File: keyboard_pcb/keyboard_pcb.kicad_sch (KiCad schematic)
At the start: 1 part

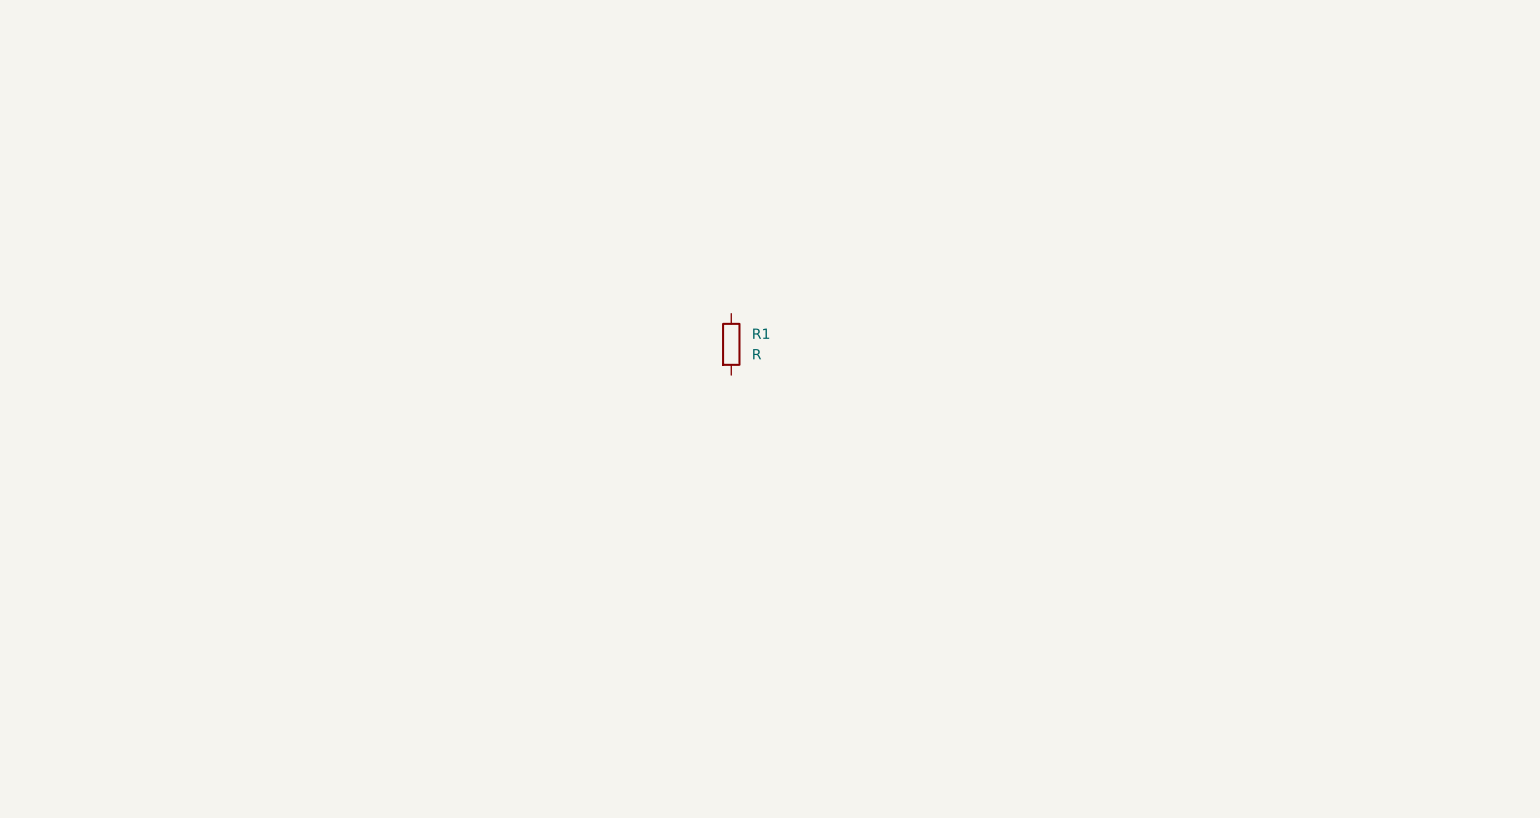
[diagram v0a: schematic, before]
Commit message: Schematic Completed, PCB drawing
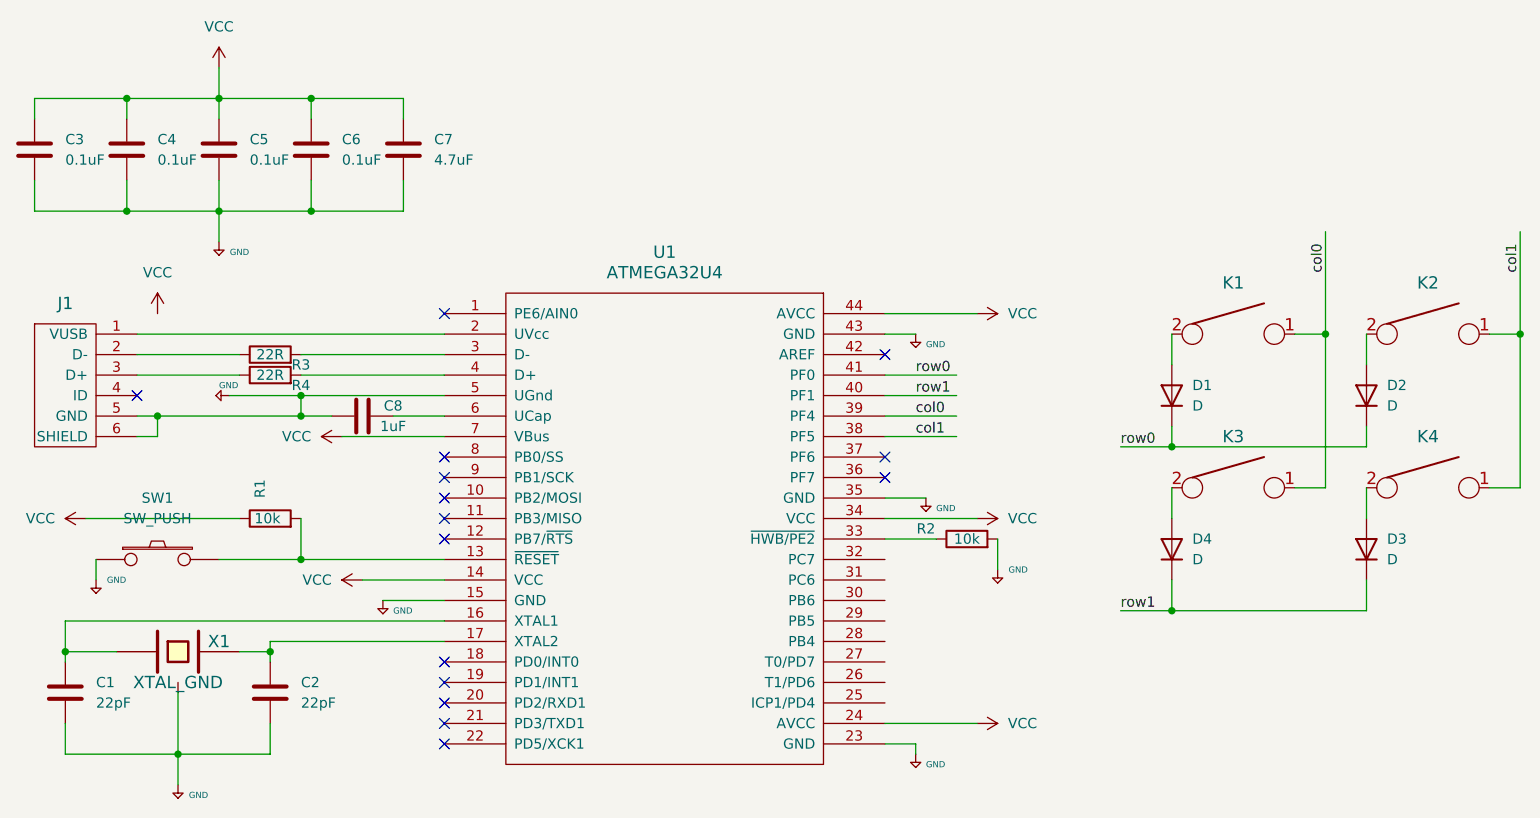
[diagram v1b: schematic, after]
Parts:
- added C1, C2: 22pF, Capacitor_SMD:C_0805_2012Metric_Pad1.18x1.45mm_HandSolder, symbol Device:C
- added C3, C4, C5, C6: 0.1uF, Capacitor_SMD:C_0805_2012Metric_Pad1.18x1.45mm_HandSolder, symbol Device:C
- added C7: 4.7uF, Capacitor_SMD:C_0805_2012Metric_Pad1.18x1.45mm_HandSolder, symbol Device:C
- added C8: 1uF, Capacitor_SMD:C_0805_2012Metric_Pad1.18x1.45mm_HandSolder, symbol Device:C
- added D1, D2, D3, D4: D, keyboard_parts:D_SOD123_axial, symbol Device:D
- added J1: USB_mini_micro_B, keyboard_parts:USB_miniB_hirose_5S8, symbol keyboard_parts:USB_mini_micro_B
- added K1, K2, K3, K4: KEYSW, keebs:Mx_Alps_100, symbol keyboard_parts:KEYSW
- added R2: 10k, Resistor_SMD:R_0805_2012Metric_Pad1.20x1.40mm_HandSolder, symbol Device:R
- added R3, R4: 22R, Resistor_SMD:R_0805_2012Metric_Pad1.20x1.40mm_HandSolder, symbol Device:R
- added SW1: SW_PUSH, Button_Switch_SMD:SW_SPST_TL3342, symbol keyboard_parts:SW_PUSH
- added U1: ATMEGA32U4, Package_QFP:LQFP-44_10x10mm_P0.8mm, symbol keyboard_parts:ATMEGA32U4
- added X1: XTAL_GND, Crystal:Crystal_SMD_3225-4Pin_3.2x2.5mm_HandSoldering, symbol keyboard_parts:XTAL_GND
- R1: value R -> 10k; footprint (none) -> Resistor_SMD:R_0805_2012Metric_Pad1.20x1.40mm_HandSolder
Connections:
- net VCC: now reaches R1.1
- net VCC: now also C3.1, C4.1, C5.1, C6.1, C7.1, U1.14 (VCC), U1.24 (AVCC), U1.34 (VCC), U1.44 (AVCC), U1.7 (VBus)
- net at R1.2: now also SW1.2, U1.13 (~{RESET})
- new net: D1.2 (A), K1.2
- new net: D2.2 (A), K2.2
- new net: C2.1, U1.17 (XTAL2), X1.2
- new net: D4.2 (A), K3.2
- new net: R2.1, U1.33 (~{HWB/PE2})
- new net: D3.2 (A), K4.2
- new net: J1.2 (D-), R3.1
- new net: R3.2, U1.3 (D-)
- new net: C1.1, U1.16 (XTAL1), X1.1
- new net: J1.1 (VUSB), U1.2 (UVcc)
- new net: J1.3 (D+), R4.1
- new net: R4.2, U1.4 (D+)
- new net: C8.2, U1.6 (UCap)
- new net +5V: C1.2, C2.2, C3.2, C4.2, C5.2, C6.2, C7.2, C8.1, J1.5 (GND), J1.6 (SHIELD), R2.2, SW1.1, U1.15 (GND), U1.23 (GND), U1.35 (GND), U1.43 (GND), U1.5 (UGnd), X1.3
- new net col0: K1.1, K3.1, U1.39 (PF4)
- new net col1: K2.1, K4.1, U1.38 (PF5)
- new net row0: D1.1 (K), D2.1 (K), U1.41 (PF0)
- new net row1: D3.1 (K), D4.1 (K), U1.40 (PF1)
- no-connect marks 0 -> 15
